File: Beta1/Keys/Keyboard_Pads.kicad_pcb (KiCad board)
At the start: 2 copper layers, 194 x 64.2 mm, 28 parts, among them U1 MPR121TH

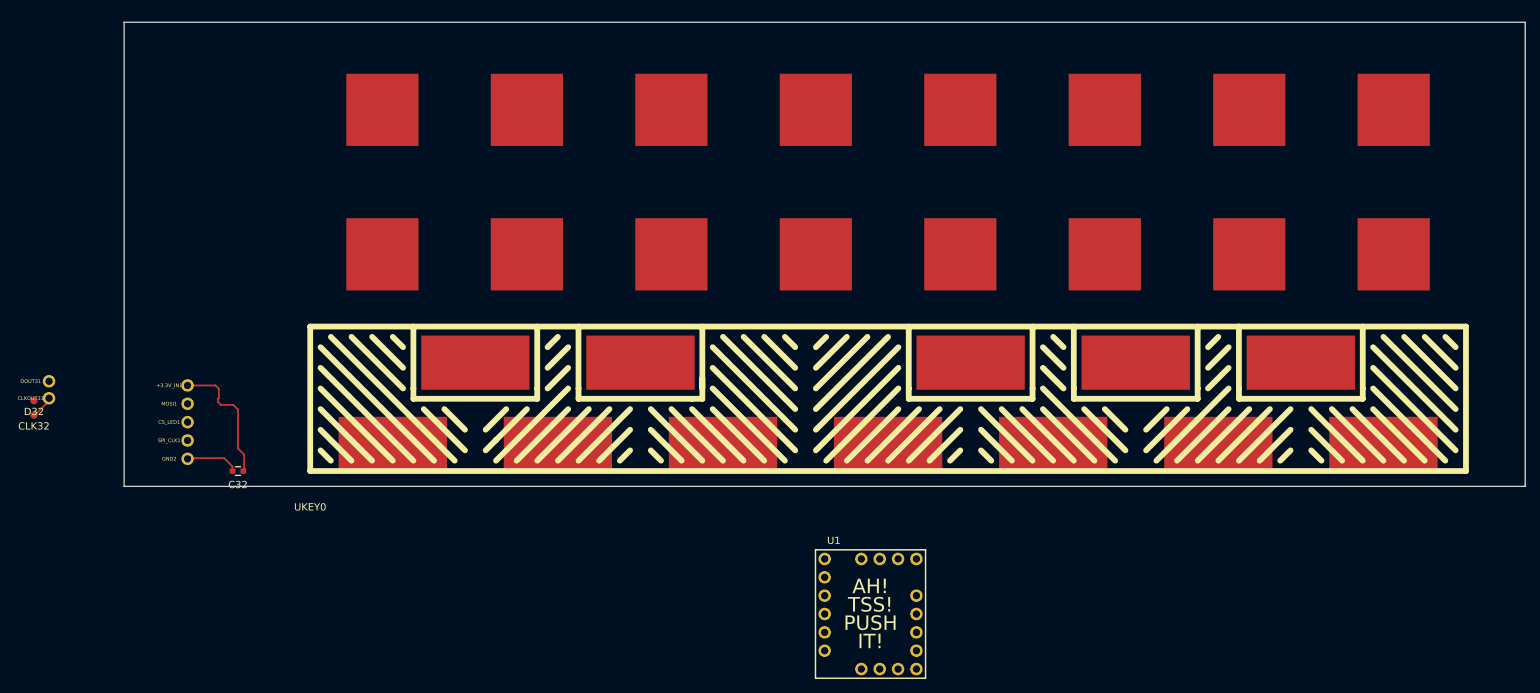
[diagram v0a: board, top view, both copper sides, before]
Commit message: Finished placement and routing of 1/2 Height Keypads. Ready to export.
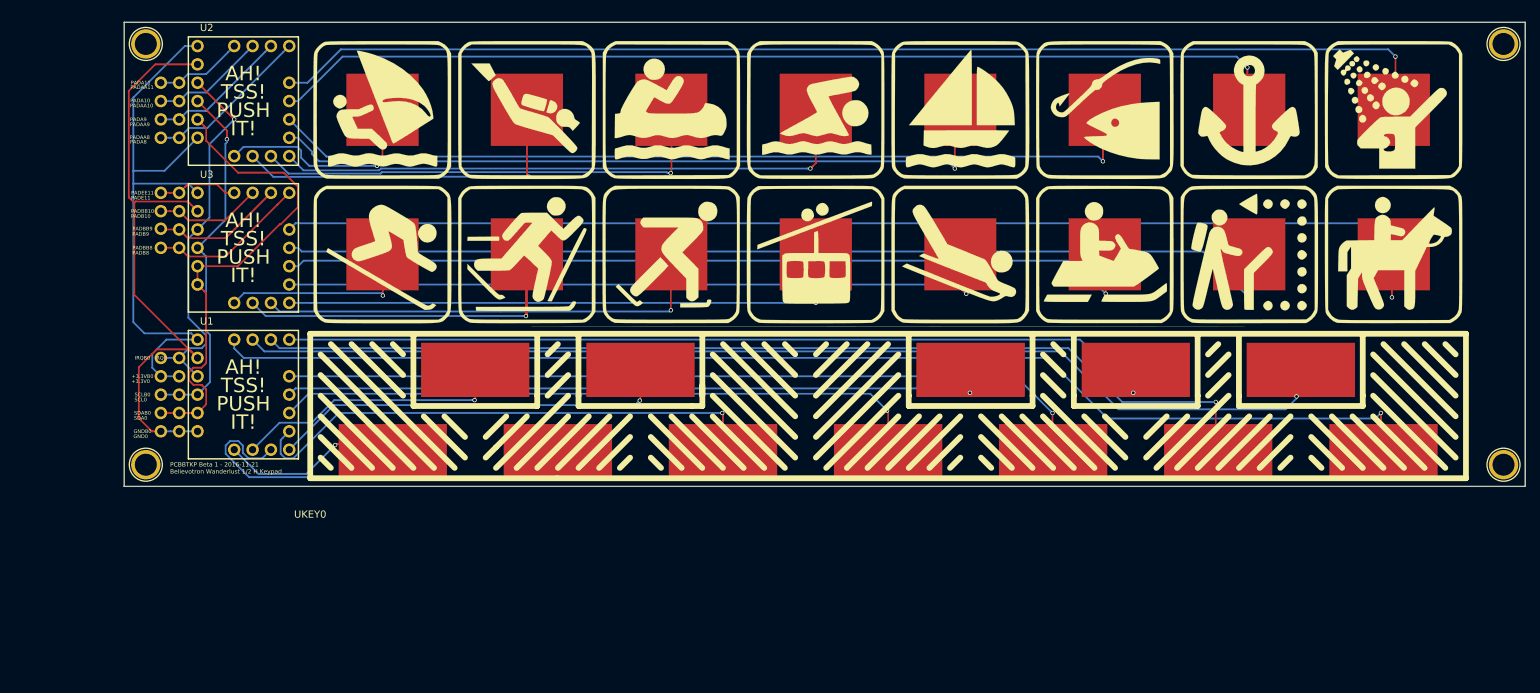
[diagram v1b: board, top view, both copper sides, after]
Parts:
- removed +3.3V_IN1, CLKOUT31, CS_LED1, DOUT31, GND2, MOSI1, SPI_CLK1: CONN_01X01, Liberry:single_0.1
- removed C32: 0.1u, Capacitors_SMD:C_0603
- removed CLK32, D32: CONN_01X01, Liberry:TESTPAD
- added +3.3V0: CONN_01X01, Liberry:single_0.1, F.Cu at (7.62, -15.2)
- added +3.3VB0: CONN_01X01, Liberry:single_0.1, F.Cu at (5.08, -15.2)
- added G***: LOGO, Liberry:Adventure_Icons_8x2_160x40, F.Cu at (105.8, -42.1)
- added GND0: CONN_01X01, Liberry:single_0.1, F.Cu at (7.62, -7.62)
- added GNDB0: CONN_01X01, Liberry:single_0.1, F.Cu at (5.08, -7.62)
- added IRQ0: CONN_01X01, Liberry:single_0.1, F.Cu at (7.62, -17.8)
- added IRQB0: CONN_01X01, Liberry:single_0.1, F.Cu at (5.08, -17.8)
- added PADA10: CONN_01X01, Liberry:single_0.1, F.Cu at (5.08, -53.3)
- added PADA11: CONN_01X01, Liberry:single_0.1, F.Cu at (5.08, -55.9)
- added PADA8: CONN_01X01, Liberry:single_0.1, F.Cu at (7.62, -48.3)
- added PADA9: CONN_01X01, Liberry:single_0.1, F.Cu at (5.08, -50.8)
- added PADAA10: CONN_01X01, Liberry:single_0.1, F.Cu at (7.62, -53.3)
- added PADAA11: CONN_01X01, Liberry:single_0.1, F.Cu at (7.62, -55.9)
- added PADAA8: CONN_01X01, Liberry:single_0.1, F.Cu at (5.08, -48.3)
- added PADAA9: CONN_01X01, Liberry:single_0.1, F.Cu at (7.62, -50.8)
- added PADB10: CONN_01X01, Liberry:single_0.1, F.Cu at (7.62, -38.1)
- added PADB8: CONN_01X01, Liberry:single_0.1, F.Cu at (7.62, -33.0)
- added PADB9: CONN_01X01, Liberry:single_0.1, F.Cu at (7.62, -35.6)
- added PADBB10: CONN_01X01, Liberry:single_0.1, F.Cu at (5.08, -38.1)
- added PADBB8: CONN_01X01, Liberry:single_0.1, F.Cu at (5.08, -33.0)
- added PADBB9: CONN_01X01, Liberry:single_0.1, F.Cu at (5.08, -35.7)
- added PADE11: CONN_01X01, Liberry:single_0.1, F.Cu at (7.62, -40.6)
- added PADEE11: CONN_01X01, Liberry:single_0.1, F.Cu at (5.08, -40.6)
- added REF**: 1pin, Connect:1pin, F.Cu at (3.00, -3.00)
- added REF**: 1pin, Connect:1pin, F.Cu at (3.00, -61.2)
- added REF**: 1pin, Connect:1pin, F.Cu at (191.0, -61.2)
- added REF**: 1pin, Connect:1pin, F.Cu at (191.0, -3.00)
- added SCL0: CONN_01X01, Liberry:single_0.1, F.Cu at (7.62, -12.7)
- added SCLB0: CONN_01X01, Liberry:single_0.1, F.Cu at (5.08, -12.7)
- added SDA0: CONN_01X01, Liberry:single_0.1, F.Cu at (7.62, -10.2)
- added SDAB0: CONN_01X01, Liberry:single_0.1, F.Cu at (5.08, -10.2)
- added U2: MPR121TH, Liberry:MPR121TH, F.Cu at (10.2, -61.0)
- added U3: MPR121TH, Liberry:MPR121TH, F.Cu at (10.2, -40.6)
- moved U1 92.0 mm to (10.2, -20.3)
- moved UKEY0 1.00 mm to (25.8, -1.12)
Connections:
- U1 pad ADDR: Net-(U1-PadADDR) -> GND
- U1 pad GND: Net-(U1-PadGND) -> GND
- U1 pad IRQ: Net-(U1-PadIRQ) -> /IRQ
- U1 pad SCL: Net-(U1-PadSCL) -> /SCL
- U1 pad SDA: Net-(U1-PadSDA) -> /SDA
- UKEY0 pad 1: Net-(UKEY0-Pad1) -> Net-(U1-PadP00)
- UKEY0 pad 10: Net-(UKEY0-Pad10) -> Net-(U1-PadP09)
- UKEY0 pad 11: Net-(UKEY0-Pad11) -> Net-(U1-PadP10)
- UKEY0 pad 12: Net-(UKEY0-Pad12) -> Net-(U1-PadP11)
- UKEY0 pad 2: Net-(UKEY0-Pad2) -> Net-(U1-PadP01)
- UKEY0 pad 3: Net-(UKEY0-Pad3) -> Net-(U1-PadP02)
- UKEY0 pad 4: Net-(UKEY0-Pad4) -> Net-(U1-PadP03)
- UKEY0 pad 5: Net-(UKEY0-Pad5) -> Net-(U1-PadP04)
- UKEY0 pad 6: Net-(UKEY0-Pad6) -> Net-(U1-PadP05)
- UKEY0 pad 7: Net-(UKEY0-Pad7) -> Net-(U1-PadP06)
- UKEY0 pad 8: Net-(UKEY0-Pad8) -> Net-(U1-PadP07)
- UKEY0 pad 9: Net-(UKEY0-Pad9) -> Net-(U1-PadP08)
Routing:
- net Net-(U1-PadP11): track 0.00 -> 168.7 mm, vias 0 -> 1
- net /PAD107: track 0.00 -> 167.2 mm, vias 0 -> 1
- net /PAD7: track 0.00 -> 162.9 mm, vias 0 -> 1
- net Net-(U1-PadP10): track 0.00 -> 154.3 mm, vias 0 -> 1
- net /PAD106: track 0.00 -> 142.0 mm, vias 0 -> 1
- net /PAD6: track 0.00 -> 141.8 mm, vias 0 -> 1
- net Net-(U1-PadP09): track 0.00 -> 140.3 mm, vias 0 -> 1
- net Net-(U1-PadP08): track 0.00 -> 124.2 mm, vias 0 -> 1
- net /PAD5: track 0.00 -> 122.3 mm, vias 0 -> 1
- net /PAD105: track 0.00 -> 120.7 mm, vias 0 -> 1
- net Net-(U1-PadP07): track 0.00 -> 112.1 mm, vias 0 -> 1
- net /PAD4: track 0.00 -> 102.5 mm, vias 0 -> 1
- net /PAD104: track 0.00 -> 100.0 mm, vias 0 -> 1
- net Net-(U1-PadP06): track 0.00 -> 99.1 mm, vias 0 -> 1
- net Net-(U1-PadP05): track 0.00 -> 89.5 mm, vias 0 -> 1
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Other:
- board text added: "PCBBTKP Beta 1 - 2016-11-21 Believotron Wanderlust 1/2 H Keypad"

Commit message: Catchup Commit.  Non-atomic, Refactored LED, Keyboard, KeyPAD, and Knobs PCBs
LED: Changed chips. Cleaned up silkscreen text. Added some support
mounting holes. Shrank height of board to avoid stackup. KeyPAD is
updated with new footprint. Keyboard and Knobs are unknown.
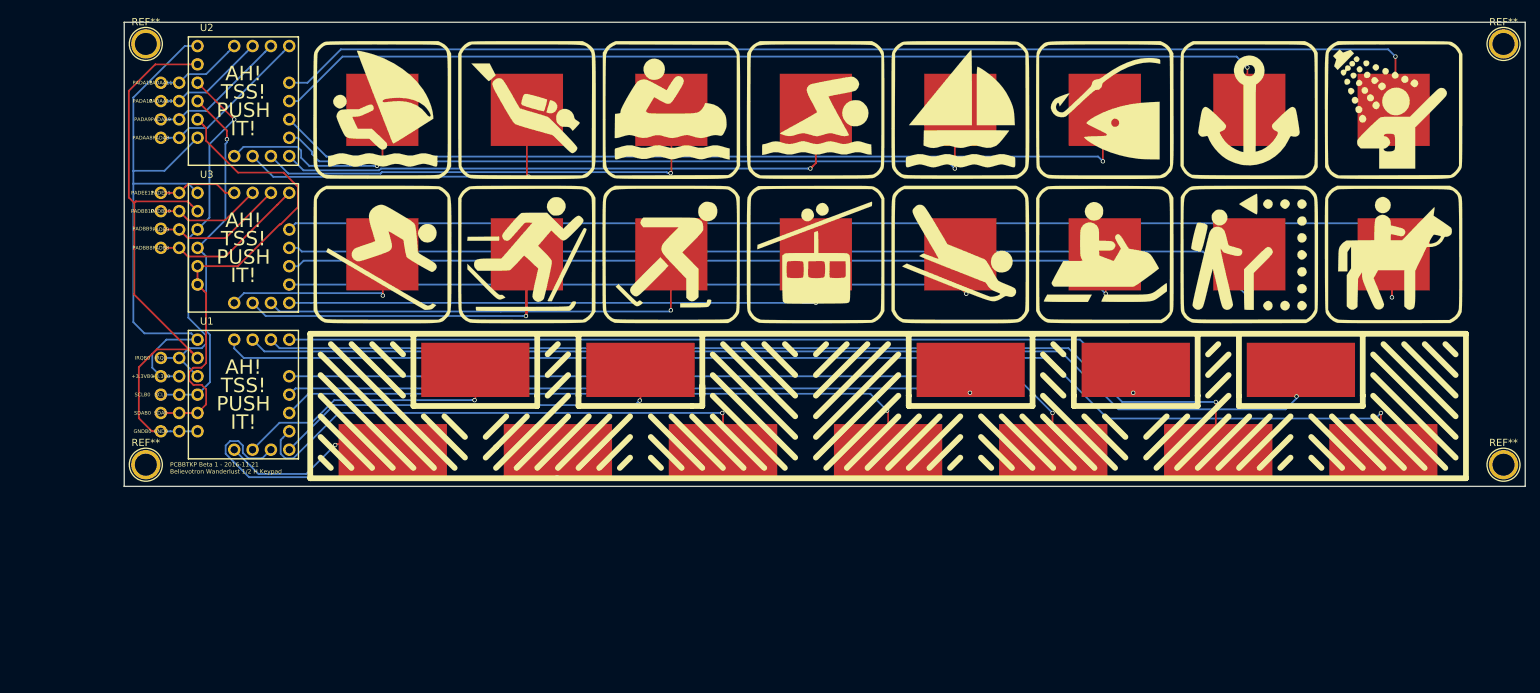
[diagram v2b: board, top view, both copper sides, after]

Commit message: Minor Fuss. Apologies.
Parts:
- removed PADA10, PADA11, PADA8, PADA9, PADAA10, PADAA11, PADAA8, PADAA9, PADB10, PADB8, PADB9, PADBB10, PADBB8, PADBB9, PADE11, PADEE11: CONN_01X01, Liberry:single_0.1
- added +3.3VA0: CONN_01X01, Liberry:single_0.1, F.Cu at (7.62, -55.9)
- added +3.3VC0: CONN_01X01, Liberry:single_0.1, F.Cu at (12.7, -55.9)
- added GNDA0: CONN_01X01, Liberry:single_0.1, F.Cu at (7.62, -45.7)
- added GNDC0: CONN_01X01, Liberry:single_0.1, F.Cu at (12.7, -45.7)
- added IRQA0: CONN_01X01, Liberry:single_0.1, F.Cu at (7.62, -53.3)
- added IRQC0: CONN_01X01, Liberry:single_0.1, F.Cu at (12.7, -53.3)
- added REF**: 1pin, Connect:1pin, F.Cu at (20.3, -2.54)
- added REF**: 1pin, Connect:1pin, F.Cu at (8.64, -39.6)
- added SCLA0: CONN_01X01, Liberry:single_0.1, F.Cu at (7.62, -48.3)
- added SCLC0: CONN_01X01, Liberry:single_0.1, F.Cu at (12.7, -48.3)
- added SDAA0: CONN_01X01, Liberry:single_0.1, F.Cu at (7.62, -50.8)
- added SDAC0: CONN_01X01, Liberry:single_0.1, F.Cu at (12.7, -50.8)
- U1, U2, U3: value MPR121TH -> MPR121OTS; footprint Liberry:MPR121TH -> Liberry:MPR121OTS
- moved U2 46.0 mm to (15.2, -15.2)
- moved +3.3VB0 41.0 mm to (10.2, -55.9)
- moved SDAB0 41.0 mm to (10.2, -50.8)
- moved +3.3V0 40.7 mm to (5.08, -55.9)
- moved SDA0 40.7 mm to (5.08, -50.8)
- moved GNDB0 38.4 mm to (10.2, -45.7)
- moved GND0 38.2 mm to (5.08, -45.7)
- moved U3 38.1 mm to (10.2, -2.54)
- moved IRQB0 35.9 mm to (10.2, -53.3)
- moved SCLB0 35.9 mm to (10.2, -48.3)
- moved IRQ0 35.7 mm to (5.08, -53.3)
- moved SCL0 35.7 mm to (5.08, -48.3)
- moved U1 14.4 mm to (20.3, -30.5)
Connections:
- PAD100 pad 1: /PAD100 -> Net-(PAD100-Pad1)
- PAD101 pad 1: /PAD101 -> Net-(PAD101-Pad1)
- PAD102 pad 1: /PAD102 -> Net-(PAD102-Pad1)
- PAD103 pad 1: /PAD103 -> Net-(PAD103-Pad1)
- PAD104 pad 1: /PAD104 -> Net-(PAD104-Pad1)
- PAD105 pad 1: /PAD105 -> Net-(PAD105-Pad1)
- PAD106 pad 1: /PAD106 -> Net-(PAD106-Pad1)
- PAD107 pad 1: /PAD107 -> Net-(PAD107-Pad1)
- U1 pad P00: Net-(U1-PadP00) -> /PAD0
- U1 pad P01: Net-(U1-PadP01) -> /PAD1
- U1 pad P02: Net-(U1-PadP02) -> /PAD2
- U1 pad P03: Net-(U1-PadP03) -> /PAD3
- U1 pad P04: Net-(U1-PadP04) -> /PAD4
- U1 pad P05: Net-(U1-PadP05) -> /PAD5
- U1 pad P06: Net-(U1-PadP06) -> /PAD6
- U1 pad P07: Net-(U1-PadP07) -> /PAD7
- U2 pad P00: /PAD0 -> Net-(PAD100-Pad1)
- U2 pad P01: /PAD1 -> Net-(PAD101-Pad1)
- U2 pad P02: /PAD2 -> Net-(PAD102-Pad1)
- U2 pad P03: /PAD3 -> Net-(PAD103-Pad1)
- U2 pad P04: /PAD4 -> Net-(PAD104-Pad1)
- U2 pad P05: /PAD5 -> Net-(PAD105-Pad1)
- U2 pad P06: /PAD6 -> Net-(PAD106-Pad1)
- U2 pad P07: /PAD7 -> Net-(PAD107-Pad1)
- U3 pad P00: /PAD100 -> Net-(U3-PadP00)
- U3 pad P01: /PAD101 -> Net-(U3-PadP01)
- U3 pad P02: /PAD102 -> Net-(U3-PadP02)
- U3 pad P03: /PAD103 -> Net-(U3-PadP03)
- U3 pad P04: /PAD104 -> Net-(U3-PadP04)
- U3 pad P05: /PAD105 -> Net-(U3-PadP05)
- U3 pad P06: /PAD106 -> Net-(U3-PadP06)
- U3 pad P07: /PAD107 -> Net-(U3-PadP07)
- U3 pad P08: Net-(PADB8-Pad1) -> Net-(U3-PadP08)
- U3 pad P09: Net-(PADB9-Pad1) -> Net-(U3-PadP09)
- U3 pad P10: Net-(PADB10-Pad1) -> Net-(U3-PadP10)
- U3 pad P11: Net-(PADE11-Pad1) -> Net-(U3-PadP11)
- UKEY0 pad 1: Net-(U1-PadP00) -> Net-(U3-PadP00)
- UKEY0 pad 10: Net-(U1-PadP09) -> Net-(U3-PadP09)
- UKEY0 pad 11: Net-(U1-PadP10) -> Net-(U3-PadP10)
- UKEY0 pad 12: Net-(U1-PadP11) -> Net-(U3-PadP11)
- UKEY0 pad 2: Net-(U1-PadP01) -> Net-(U3-PadP01)
- UKEY0 pad 3: Net-(U1-PadP02) -> Net-(U3-PadP02)
- UKEY0 pad 4: Net-(U1-PadP03) -> Net-(U3-PadP03)
- UKEY0 pad 5: Net-(U1-PadP04) -> Net-(U3-PadP04)
- UKEY0 pad 6: Net-(U1-PadP05) -> Net-(U3-PadP05)
- UKEY0 pad 7: Net-(U1-PadP06) -> Net-(U3-PadP06)
- UKEY0 pad 8: Net-(U1-PadP07) -> Net-(U3-PadP07)
- UKEY0 pad 9: Net-(U1-PadP08) -> Net-(U3-PadP08)
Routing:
- net Net-(PAD107-Pad1): track 0.00 -> 183.6 mm, vias 0 -> 1
- net Net-(U3-PadP11): track 0.00 -> 178.9 mm, vias 0 -> 1
- net Net-(U1-PadP11): track 168.7 -> 0.00 mm, vias 1 -> 0
- net /PAD107: track 167.2 -> 0.00 mm, vias 1 -> 0
- net Net-(U3-PadP10): track 0.00 -> 160.6 mm, vias 0 -> 1
- net Net-(U3-PadP09): track 0.00 -> 154.7 mm, vias 0 -> 1
- net Net-(U1-PadP10): track 154.3 -> 0.00 mm, vias 1 -> 0
- net Net-(PAD106-Pad1): track 0.00 -> 152.8 mm, vias 0 -> 1
- net /PAD106: track 142.0 -> 0.00 mm, vias 1 -> 0
- net Net-(U1-PadP09): track 140.3 -> 0.00 mm, vias 1 -> 0
- net Net-(U3-PadP08): track 0.00 -> 140.0 mm, vias 0 -> 1
- net Net-(U3-PadP07): track 0.00 -> 129.0 mm, vias 0 -> 1
- net Net-(PAD105-Pad1): track 0.00 -> 127.7 mm, vias 0 -> 1
- net Net-(U1-PadP08): track 124.2 -> 0.00 mm, vias 1 -> 0
- net /PAD105: track 120.7 -> 0.00 mm, vias 1 -> 0
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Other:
- board size 194 x 64.2 mm -> 194 x 64 mm
- board text added: "Once upon a time, there was a you, and you made the most beautiful frequencies. The darkness-at-the-end-of-the-universe quakes in agony at the beauty it will miss when your vibrations and their effects cease their joyful excitations."
- board text added: "PCBBTKP Beta 1 - 2016-12-20 Believotron Wanderlust 1/2 H Keypad"
- board text removed: "PCBBTKP Beta 1 - 2016-11-21 Believotron Wanderlust 1/2 H Keypad"

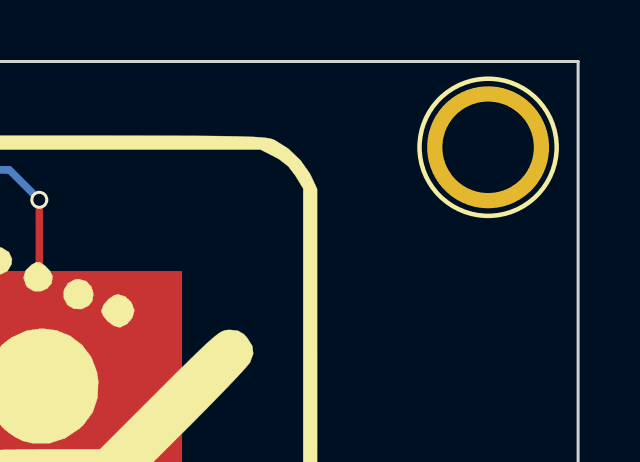
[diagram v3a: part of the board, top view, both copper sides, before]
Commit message: Moved mounting hole in by 2.54 mm to see if it would work.
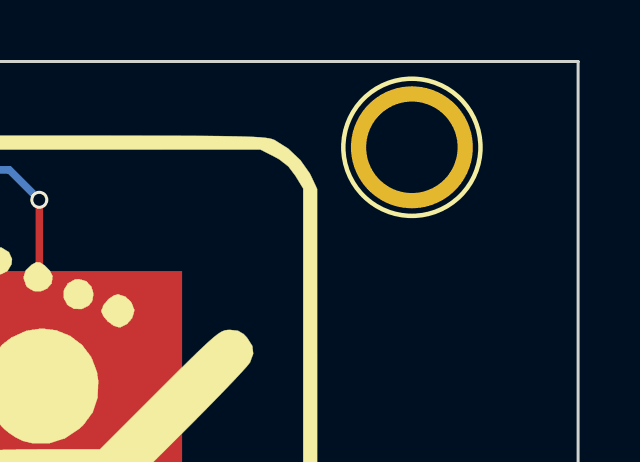
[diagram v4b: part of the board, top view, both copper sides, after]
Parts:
- moved REF** 2.54 mm to (188.4, -61.2)
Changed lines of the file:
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@@
     (links 46)
     (no_connects 0)
-    (area -0.050001 -64.160001 194.010001 -0.089999)
+    (area -0.050001 -65.273 194.010001 7.95)
     (thickness 1.6)
     (drawings 19)
@@
   )
   (module Connect:1pin (layer F.Cu)
-    (at 190.96 -61.25)
+    (at 188.42 -61.25)
     (descr "module 1 pin (ou trou mecanique de percage)")
     (tags DEV)
